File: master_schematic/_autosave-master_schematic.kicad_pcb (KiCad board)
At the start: 4 copper layers, 157.5 x 111.9 mm, 82 parts, among them J1 Conn_01x02_Shielded, J10 0430450400, J11 1723103102, J12 1723103102, J13 1723103102, J14 1723103102, J15 1723103102, J16 1723103102, J17 1723103102, J18 1723103102, J19 1723103102, J2 0430450400, J20 1723103102, J3 0430450400, J4 0430450400, J5 0430450400, J6 0430450400, J7 0430450400, J8 0430450400, J9 0430450400, Q1 CWDM3011N TR13 PBFREE, Q10 CWDM3011N TR13 PBFREE, Q2 CWDM3011N TR13 PBFREE, Q3 CWDM3011N TR13 PBFREE, Q4 CWDM3011N TR13 PBFREE, Q5 CWDM3011N TR13 PBFREE, Q6 CWDM3011N TR13 PBFREE, Q7 CWDM3011N TR13 PBFREE, Q8 CWDM3011N TR13 PBFREE, Q9 CWDM3011N TR13 PBFREE, U1 RFM95, U10 HX711, U11 HX711, U2 teensy_4.1, U4 MCP9600_Module, U5 MCP9600_Module, U6 MCP9600_Module, U7 MCP9600_Module, U8 MCP9600_Module, U9 HX711

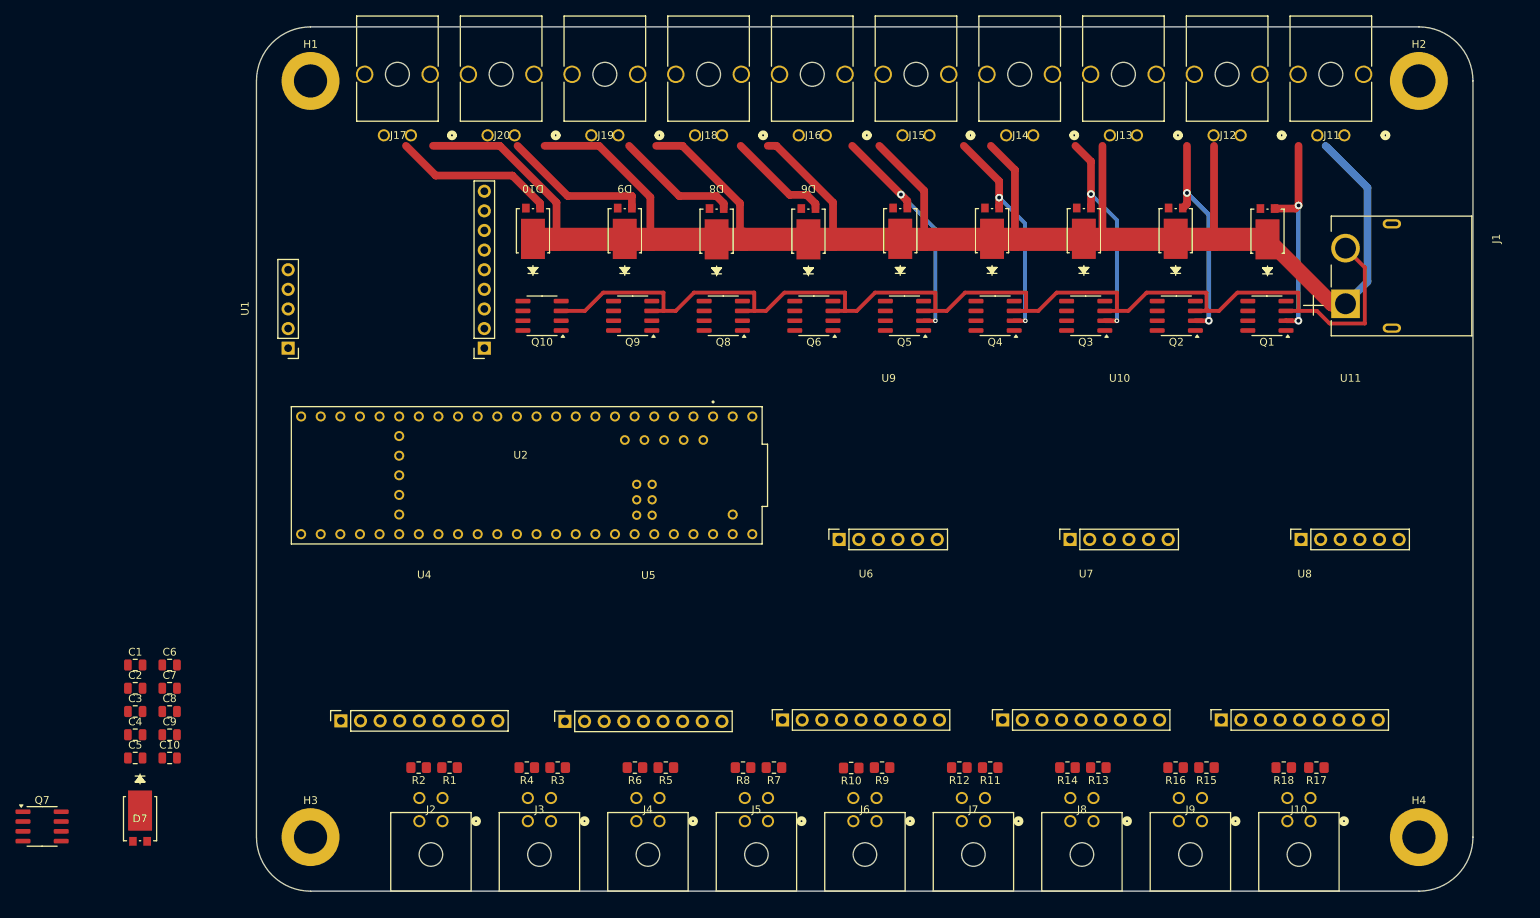
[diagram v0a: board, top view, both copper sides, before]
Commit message: added decoupling capacitors, fixed voltage values for TTs and load cells to +3V3
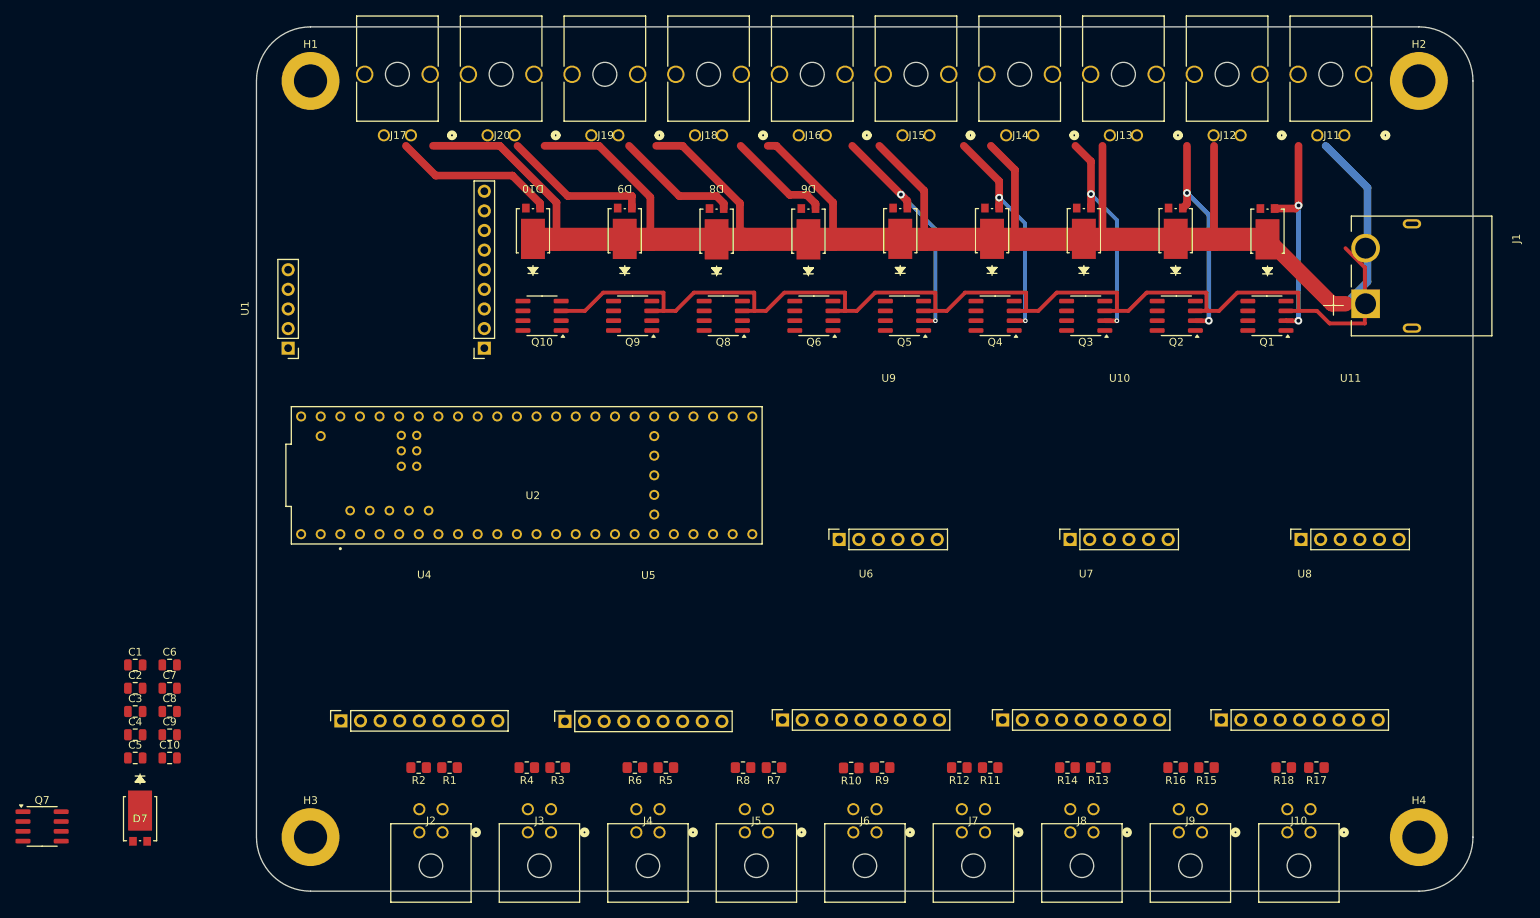
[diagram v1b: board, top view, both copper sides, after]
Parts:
- moved J1 2.60 mm to (174.6, 53.2)
- moved J10 1.45 mm to (161.5, 125.3)
- moved J2 1.45 mm to (49.1, 125.3)
- moved J3 1.45 mm to (63.1, 125.3)
- moved J4 1.45 mm to (77.2, 125.3)
- moved J5 1.45 mm to (91.2, 125.3)
- moved J6 1.45 mm to (105.3, 125.3)
- moved J7 1.45 mm to (119.3, 125.3)
- moved J8 1.45 mm to (133.4, 125.3)
- moved J9 1.45 mm to (147.4, 125.3)
- turned U2 to 0 degrees
